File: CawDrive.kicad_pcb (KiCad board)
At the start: 4 copper layers, 40 x 40 mm, 83 parts, among them J1 Conn_01x11_Pin, J4 Conn_01x07_Pin, Q10 TPH3R704PL, Q11 TPH3R704PL, Q12 TPH3R704PL, Q7 TPH3R704PL, Q8 TPH3R704PL, Q9 TPH3R704PL, U1 STM32F446RETx, U2 TLV76733DRVR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

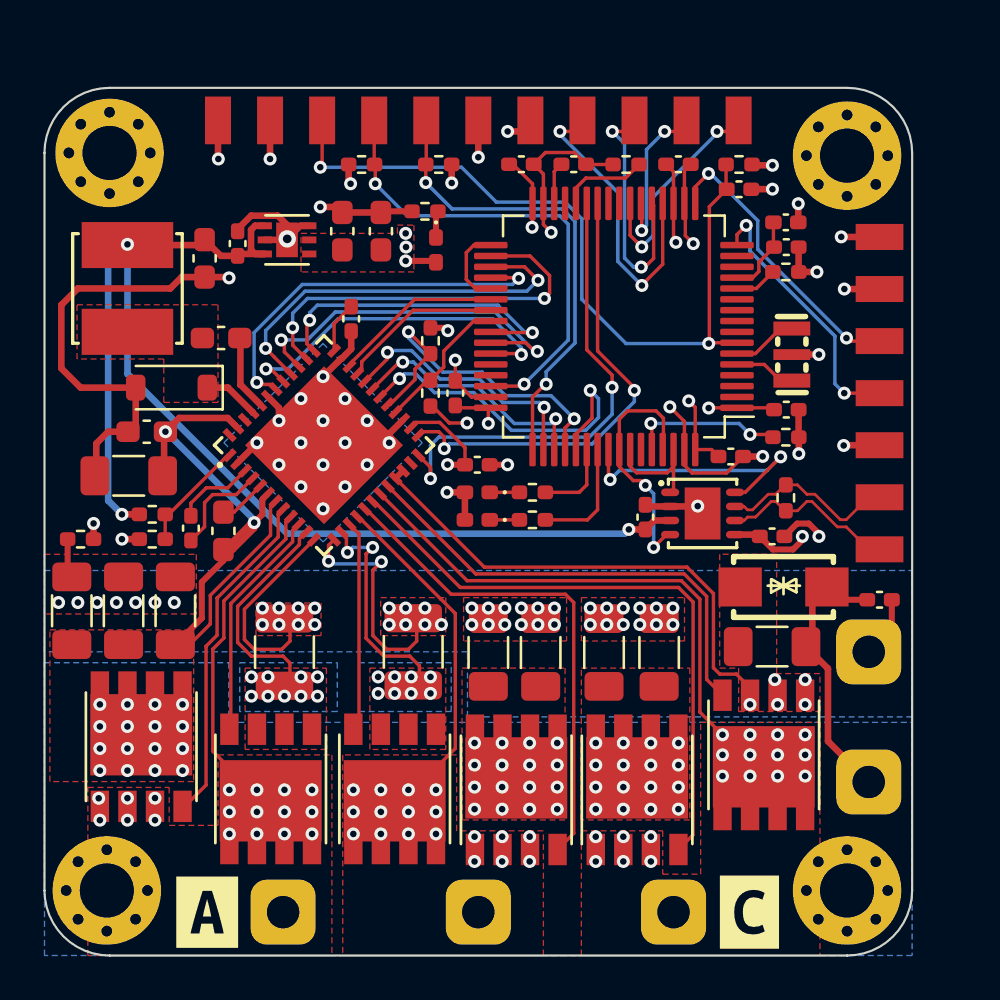
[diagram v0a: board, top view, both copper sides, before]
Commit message: 升级主控STM32G474，增加AS5047P编码器，支持NTC温度采样
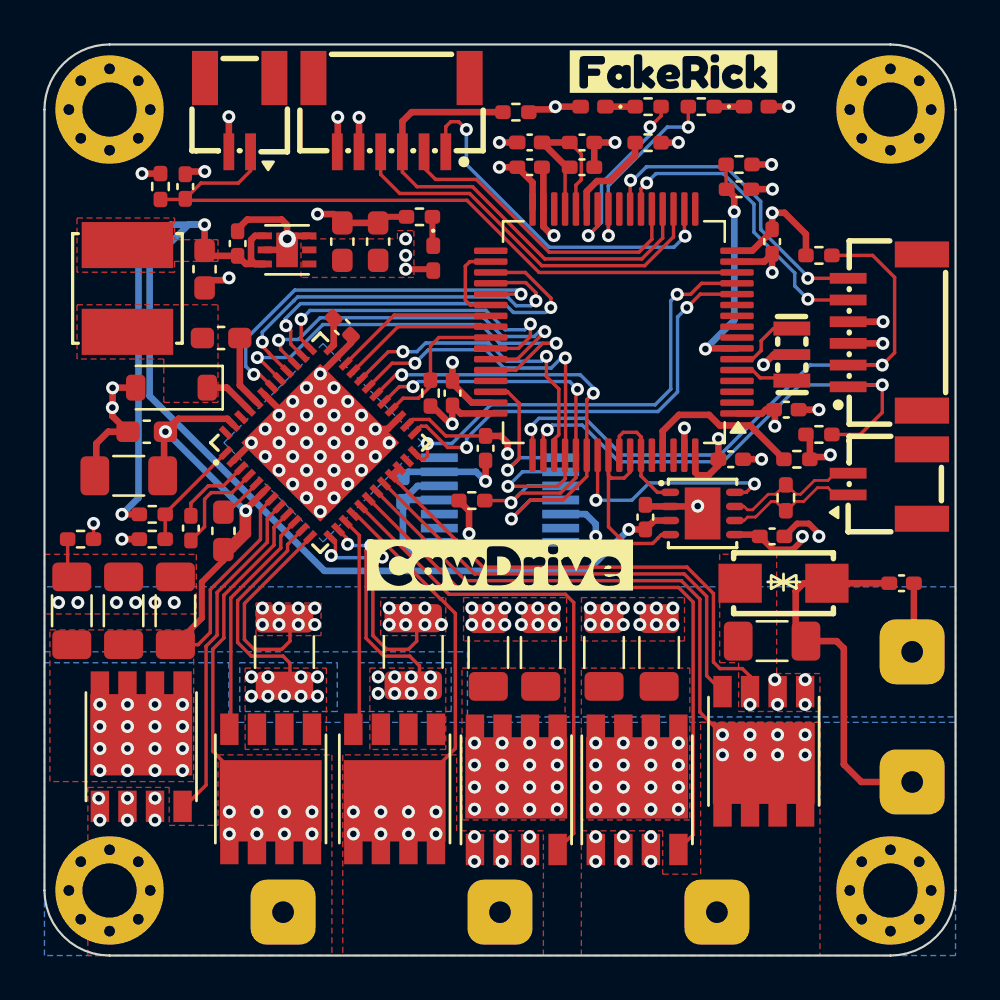
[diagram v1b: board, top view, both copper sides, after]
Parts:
- removed G***: LOGO, Rick_Logo:guaik_logo_black_7x7
- removed J1: Conn_01x11_Pin, CawDrive_Connector:SOIC-11
- removed J4: Conn_01x07_Pin, CawDrive_Connector:SOIC-7
- removed R3, R5, R6: 10k, Resistor_SMD:R_0402_1005Metric_Pad0.72x0.64mm_HandSolder
- removed kibuzzard-65071042: G***, kibuzzard-65071042
- removed kibuzzard-650713F8: G***, kibuzzard-650713F8
- removed kibuzzard-65072293: G***, kibuzzard-65072293
- removed kibuzzard-650722BD: G***, kibuzzard-650722BD
- removed kibuzzard-651AD87F: G***, kibuzzard-651AD87F
- removed kibuzzard-651BBA97: G***, kibuzzard-651BBA97
- added C11: 0.1uF, Capacitor_SMD:C_0402_1005Metric_Pad0.74x0.62mm_HandSolder, F.Cu at (144.8, 72.5)
- added C17: 0.1uF, Capacitor_SMD:C_0402_1005Metric_Pad0.74x0.62mm_HandSolder, B.Cu at (136.5, 88.5)
- added CN1: WAFER-SH1.0-6PWB, Rick_Connector:CONN-SMD_6P-P1.00_XUNPU_WAFER-SH1.0-6PWB, F.Cu at (136.0, 71.2)
- added CN2: WAFER-SH1.0-6PWB, Rick_Connector:CONN-SMD_6P-P1.00_XUNPU_WAFER-SH1.0-6PWB, F.Cu at (158.8, 81.3)
- added R12: 10K, Resistor_SMD:R_0402_1005Metric_Pad0.72x0.64mm_HandSolder, F.Cu at (154.7, 87.1)
- added R15: 0Ω, Resistor_SMD:R_0402_1005Metric_Pad0.72x0.64mm_HandSolder, F.Cu at (147.8, 72.5)
- added R20: 10k, Resistor_SMD:R_0402_1005Metric_Pad0.72x0.64mm_HandSolder, F.Cu at (155.7, 77.7)
- added R21: 10k, Resistor_SMD:R_0402_1005Metric_Pad0.72x0.64mm_HandSolder, F.Cu at (155.7, 86.0)
- added U4: STM32G474RETx, Package_QFP:LQFP-64_10x10mm_P0.5mm, F.Cu at (146.2, 81.3)
- added U6: WAFER-SH1.0-2PWB, Rick_Connector:CONN-SMD_2P-P1.00_XUNPU_WAFER-SH1.0-2PWB, F.Cu at (129.0, 71.2)
- added U7: DRV8323RSRGZR, Rick_Drive:DRV8323RS_QFN-48-EP(7x7), F.Cu at (132.7, 86.4)
- added kibuzzard-66ADBF8B: G***, kibuzzard-66ADBF8B, F.Cu at (149.0, 69.2)
- added kibuzzard-66ADCBBA: G***, kibuzzard-66ADCBBA, F.Cu at (141.0, 92.0)
- C1: value 2.2uF -> 0.1uF
- R1: value 10K -> 10k
- R18, R19: value 1mΩ -> 1mΩ 1%
- R2: value 0Ω -> 10k
- R8: value 120 -> 120Ω 1%
- U1: value STM32F446RETx -> AS5047P-ATSM; footprint Package_QFP:LQFP-64_10x10mm_P0.5mm -> Rick_Sensor:AS5047P-ATSM; moved to B.Cu
- U5: value DRV8323RSRGZR -> WAFER-SH1.0-2PWB; footprint Rick_Drive:DRV8323RS_QFN-48-EP(7x7) -> Rick_Connector:CONN-SMD_2P-P1.00_XUNPU_WAFER-SH1.0-2PWB
- moved R1 31.1 mm to (125.3, 74.5), turned to 90 degrees
- moved U5 25.9 mm to (158.8, 88.3), turned to 90 degrees
- moved D2 23.0 mm to (152.8, 70.9), turned to 0 degrees
- moved R11 20.6 mm to (150.3, 70.9), turned to 180 degrees
- moved D1 18.6 mm to (145.3, 70.9)
- moved R9 18.6 mm to (147.8, 70.9)
- moved C1 17.9 mm to (126.5, 74.5), turned to -90 degrees
- moved R2 14.5 mm to (141.7, 71.1), turned to 180 degrees
- moved L1 12.4 mm to (142.4, 72.5), turned to 0 degrees
- moved C8 10.1 mm to (144.8, 73.7)
- moved U1 9.57 mm to (141.0, 89.0), turned to -90 degrees
- moved R16 7.61 mm to (139.7, 89.0), turned to 0 degrees
- moved C3 5.60 mm to (153.5, 77.1), turned to -90 degrees
- moved H2 2.92 mm to (159.0, 71.0)
- moved H1 2.00 mm to (123.0, 71.0)
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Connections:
- C1 pad 1: Net-(U1-VCAP_1) -> GND
- C1 pad 2: GND -> /ADC1_IN3
- C27 pad 1: Net-(U5-CPL) -> Net-(U7-CPL)
- C27 pad 2: Net-(U5-CPH) -> Net-(U7-CPH)
- C28 pad 2: Net-(U5-VCP) -> Net-(U7-VCP)
- C31 pad 1: Net-(U5-DVDD) -> Net-(U7-DVDD)
- R1 pad 1: GND -> /ADC1_IN3
- R1 pad 2: Net-(U1-BOOT0) -> +3.3V
- R2 pad 1: Net-(U1-VSSA) -> +3.3V
- R2 pad 2: GND -> /SPI1_MISO
- U1 pad 1: +3.3V -> /AS5047P_NSS
- U1 pad 11: unconnected-(U1-PC3-Pad11) -> +3.3V
- U1 pad 12: Net-(U1-VSSA) -> +3.3V
- U1 pad 13: +3.3VA -> GND
- U1 pad 2: unconnected-(U1-PC13-Pad2) -> /SPI3_SCK
- U1 pad 3: unconnected-(U1-PC14-Pad3) -> /SPI3_MISO
- U1 pad 4: unconnected-(U1-PC15-Pad4) -> /SPI3_MOSI
- U1 pad 5: /HSE_IN -> GND
- U1 pad 6: /HSE_OUT -> unconnected-(U1-B-Pad6)
- U1 pad 7: /RESET -> unconnected-(U1-A-Pad7)
- U3 pad 1: /CAN_TX -> /FDCAN_TX
- U3 pad 4: /CAN_RX -> /FDCAN_RX
- U3 pad 8: /CAN_STB -> /FDCAN_STB
- U5 pad 1: /DRV8323RSRGZR/FB -> /CAN_N
- U5 pad 2: GND -> /CAN_P
- U5 pad 3: Net-(U5-CPL) -> unconnected-(U5-Pad3)
- U5 pad 4: Net-(U5-CPH) -> unconnected-(U5-Pad4)
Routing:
- net /ADC1_IN3: track 0.00 -> 32.4 mm
- net /RESET: track 35.6 -> 10.7 mm
- net /ADC1_IN9: track 22.0 -> 0.00 mm, vias 2 -> 0
- net /ADC1_IN8: track 21.4 -> 0.00 mm, vias 2 -> 0
- net /ADC1_IN2: track 0.00 -> 21.1 mm, vias 0 -> 2
- net /ADC1_IN1: track 0.00 -> 20.6 mm, vias 0 -> 2
- net /TIM1_CH3: track 0.00 -> 19.7 mm, vias 0 -> 2
- net /TIM1_CH1N: track 0.00 -> 18.5 mm, vias 0 -> 2
- net /TIM1_CH2N: track 0.00 -> 18.5 mm, vias 0 -> 2
- net /TIM1_PWM_CH1N: track 18.5 -> 0.00 mm, vias 2 -> 0
- net /TIM1_PWM_CH2N: track 18.4 -> 0.00 mm, vias 2 -> 0
- net /TIM1_CH3N: track 0.00 -> 17.9 mm, vias 0 -> 2
- net /TIM1_PWM_CH3N: track 17.9 -> 0.00 mm, vias 2 -> 0
- net /TIM1_CH2: track 0.00 -> 17.6 mm, vias 0 -> 2
- net /TIM1_PWM_CH2: track 16.9 -> 0.00 mm, vias 2 -> 0
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- added copper zone on F.Cu, net +5V
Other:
- board size 40 x 40 mm -> 42 x 42 mm
